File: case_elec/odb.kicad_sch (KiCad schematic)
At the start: 4 parts

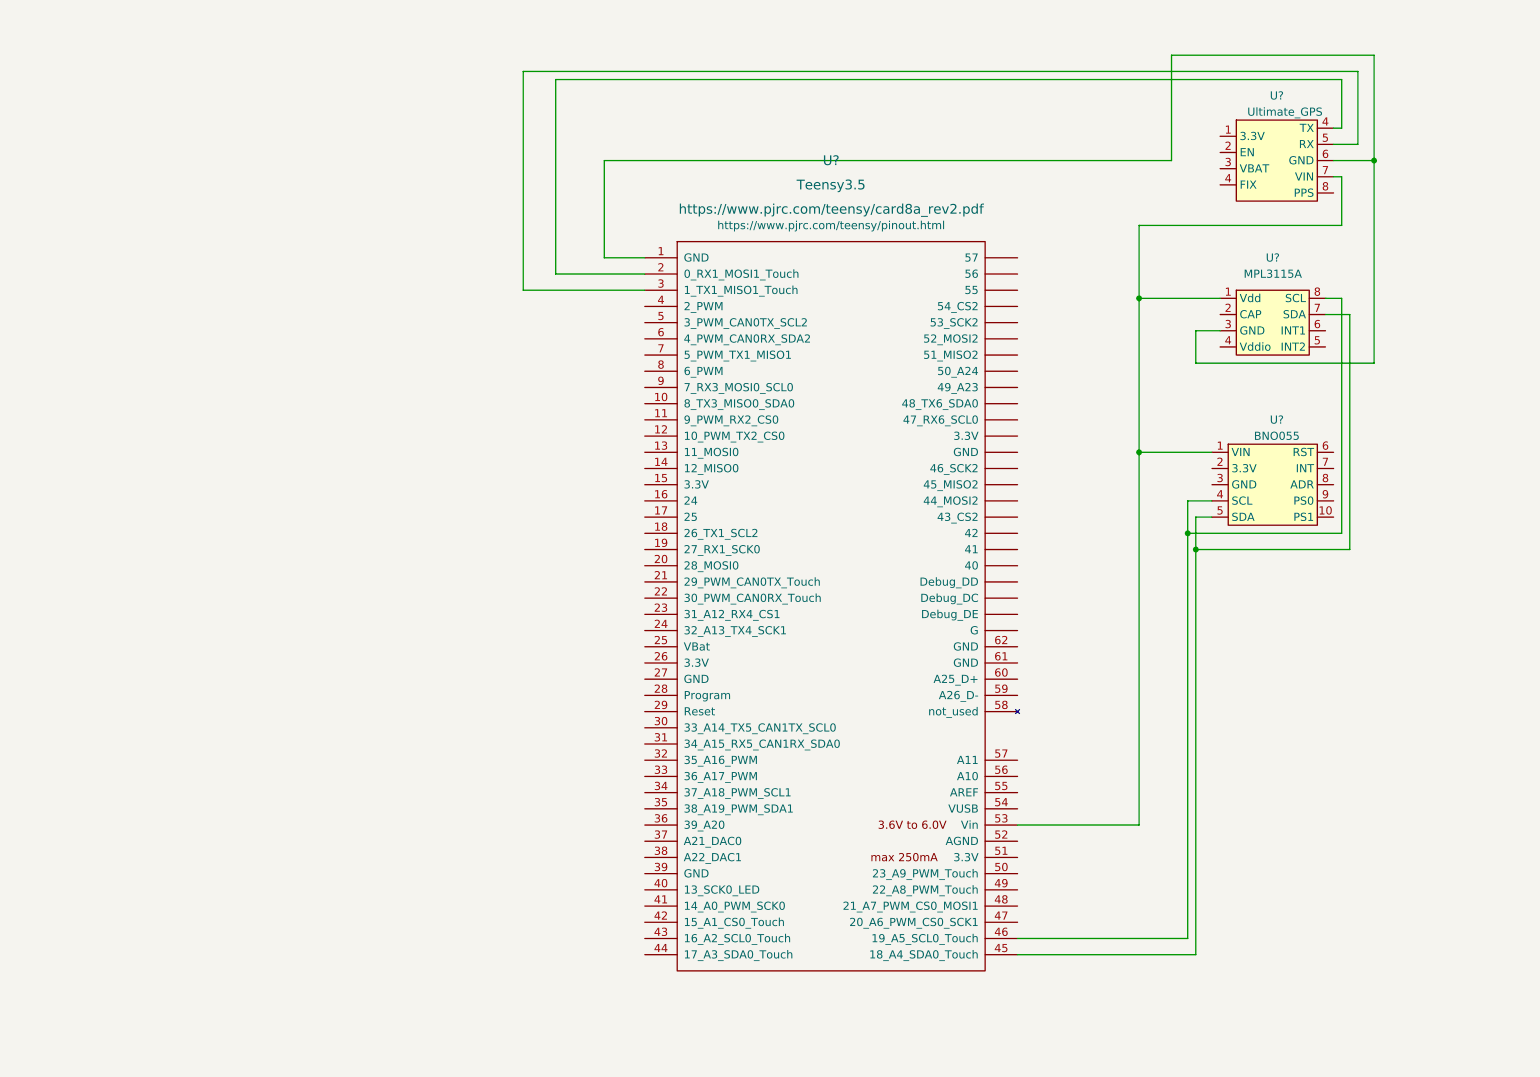
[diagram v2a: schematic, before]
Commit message: Connexion SDA/SCL
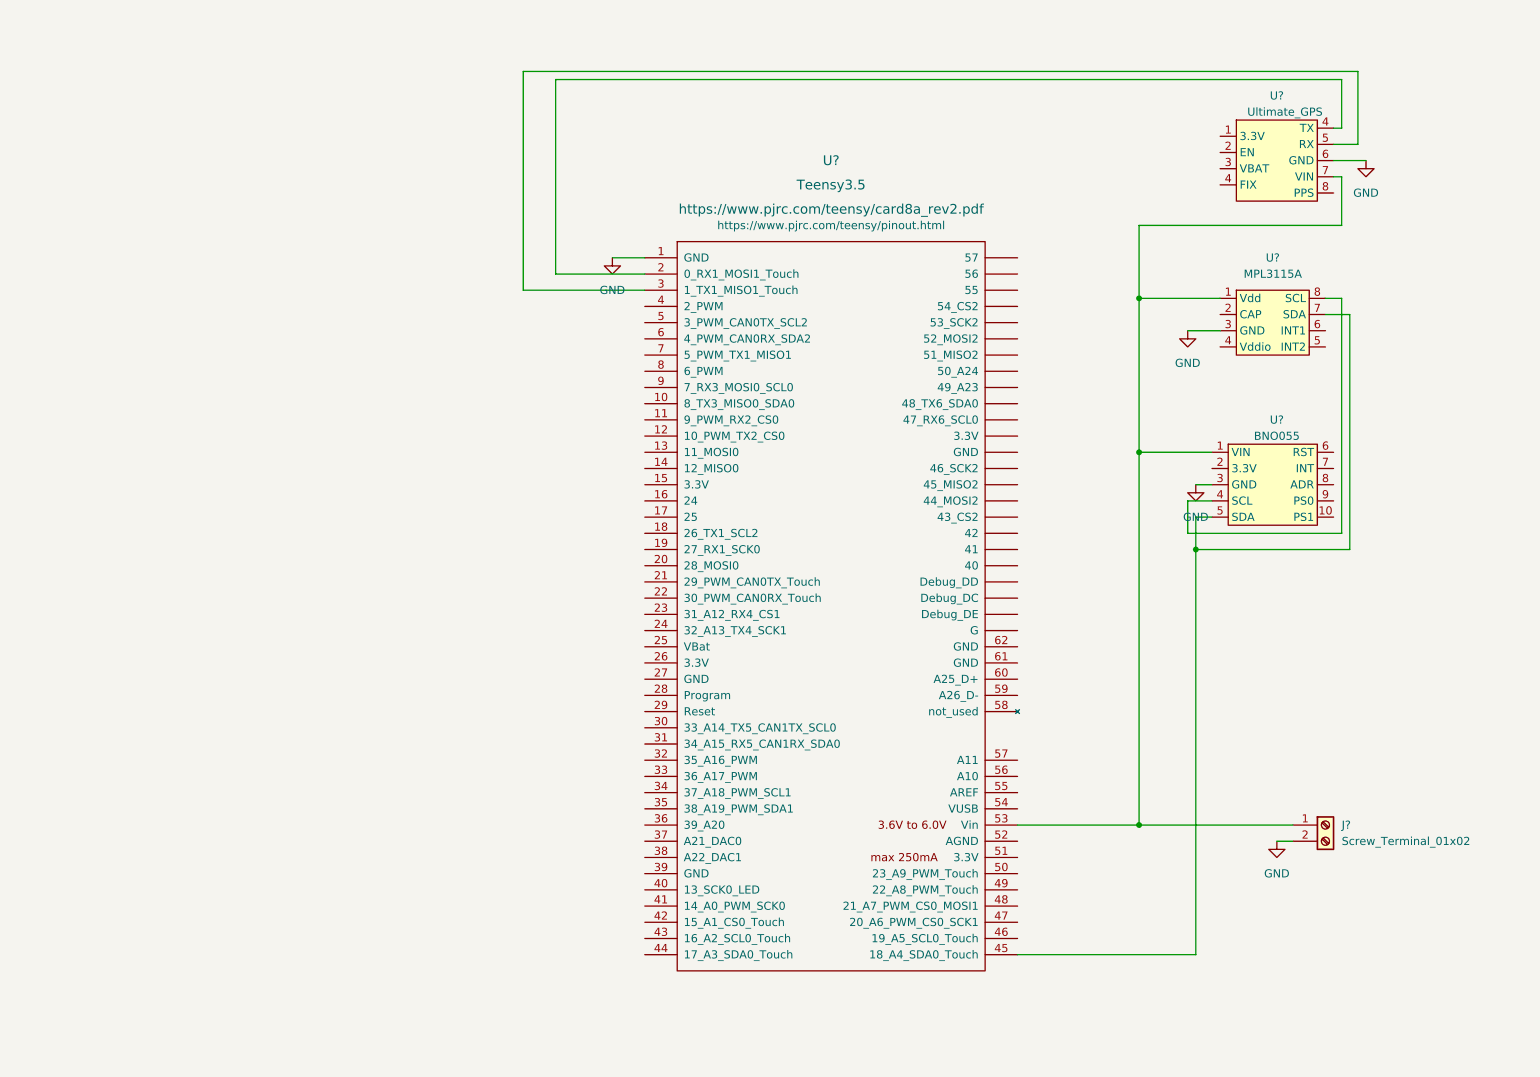
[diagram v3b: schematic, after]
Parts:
- added J?: Screw_Terminal_01x02, symbol Connector:Screw_Terminal_01x02
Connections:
- net at U?.1 (VIN), U?.1 (Vdd), U?.53 (Vin)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: now also J?.1 (Pin_1)
- net GND: now reaches U?.1 (GND), U?.3 (GND), U?.6 (GND)
- net GND: now also U?.3 (GND), J?.2 (Pin_2)
- net at U?.4 (SCL), U?.8 (SCL): no longer U?.46 (19_A5_SCL0_Touch)
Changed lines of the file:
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@@
     (comment 3 "<mohamed-iadh.bani@top-aero.com> <theo.tugaye@top-aero.com>")
   )
-  (junction (at 226.06 40.64) (diameter 0) (color 0 0 0 0)
-  )
   (junction (at 198.12 101.6) (diameter 0) (color 0 0 0 0)
   )
@@
   (junction (at 189.23 86.36) (diameter 0) (color 0 0 0 0)
   )
-  (junction (at 196.85 99.06) (diameter 0) (color 0 0 0 0)
+  (junction (at 189.23 144.78) (diameter 0) (color 0 0 0 0)
   )
   (wire (pts (xy 222.25 101.6) (xy 198.12 101.6))
@@
     (stroke (width 0) (type default) (color 0 0 0 0))
   )
-  (wire (pts (xy 198.12 67.31) (xy 198.12 72.39))
-    (stroke (width 0) (type default) (color 0 0 0 0))
-  )
-  (wire (pts (xy 201.93 67.31) (xy 198.12 67.31))
-    (stroke (width 0) (type default) (color 0 0 0 0))
-  )
   (wire (pts (xy 201.93 62.23) (xy 189.23 62.23))
     (stroke (width 0) (type default) (color 0 0 0 0))
@@
     (stroke (width 0) (type default) (color 0 0 0 0))
   )
-  (wire (pts (xy 198.12 72.39) (xy 226.06 72.39))
-    (stroke (width 0) (type default) (color 0 0 0 0))
-  )
-  (wire (pts (xy 194.31 40.64) (xy 194.31 24.13))
+  (wire (pts (xy 196.85 67.31) (xy 201.93 67.31))
+    (stroke (width 0) (type default) (color 0 0 0 0))
+  )
+  (wire (pts (xy 106.68 55.88) (xy 111.76 55.88))
     (stroke (width 0) (type default) (color 0 0 0 0))
   )
@@
     (stroke (width 0) (type default) (color 0 0 0 0))
   )
-  (wire (pts (xy 194.31 40.64) (xy 105.41 40.64))
-    (stroke (width 0) (type default) (color 0 0 0 0))
-  )
   (wire (pts (xy 97.79 27.94) (xy 220.98 27.94))
     (stroke (width 0) (type default) (color 0 0 0 0))
@@
     (stroke (width 0) (type default) (color 0 0 0 0))
   )
-  (wire (pts (xy 105.41 55.88) (xy 111.76 55.88))
-    (stroke (width 0) (type default) (color 0 0 0 0))
-  )
   (wire (pts (xy 219.71 35.56) (xy 220.98 35.56))
     (stroke (width 0) (type default) (color 0 0 0 0))
   )
-  (wire (pts (xy 226.06 24.13) (xy 226.06 40.64))
-    (stroke (width 0) (type default) (color 0 0 0 0))
-  )
-  (wire (pts (xy 196.85 162.56) (xy 196.85 99.06))
-    (stroke (width 0) (type default) (color 0 0 0 0))
-  )
-  (wire (pts (xy 219.71 40.64) (xy 226.06 40.64))
+  (wire (pts (xy 189.23 144.78) (xy 213.36 144.78))
+    (stroke (width 0) (type default) (color 0 0 0 0))
+  )
+  (wire (pts (xy 198.12 91.44) (xy 200.66 91.44))
     (stroke (width 0) (type default) (color 0 0 0 0))
   )
@@
     (stroke (width 0) (type default) (color 0 0 0 0))
   )
-  (wire (pts (xy 170.18 162.56) (xy 196.85 162.56))
-    (stroke (width 0) (type default) (color 0 0 0 0))
-  )
   (wire (pts (xy 222.25 64.77) (xy 222.25 101.6))
     (stroke (width 0) (type default) (color 0 0 0 0))
@@
     (stroke (width 0) (type default) (color 0 0 0 0))
   )
-  (wire (pts (xy 226.06 40.64) (xy 226.06 72.39))
-    (stroke (width 0) (type default) (color 0 0 0 0))
-  )
   (wire (pts (xy 220.98 50.8) (xy 189.23 50.8))
     (stroke (width 0) (type default) (color 0 0 0 0))
   )
-  (wire (pts (xy 105.41 40.64) (xy 105.41 55.88))
-    (stroke (width 0) (type default) (color 0 0 0 0))
-  )
   (wire (pts (xy 218.44 64.77) (xy 222.25 64.77))
     (stroke (width 0) (type default) (color 0 0 0 0))
   )
-  (wire (pts (xy 194.31 24.13) (xy 226.06 24.13))
-    (stroke (width 0) (type default) (color 0 0 0 0))
-  )
   (wire (pts (xy 220.98 62.23) (xy 220.98 99.06))
     (stroke (width 0) (type default) (color 0 0 0 0))
   )
+  (wire (pts (xy 213.36 147.32) (xy 210.82 147.32))
+    (stroke (width 0) (type default) (color 0 0 0 0))
+  )
   (wire (pts (xy 198.12 96.52) (xy 200.66 96.52))
     (stroke (width 0) (type default) (color 0 0 0 0))
   )
+  (wire (pts (xy 219.71 40.64) (xy 224.79 40.64))
+    (stroke (width 0) (type default) (color 0 0 0 0))
+  )
   (wire (pts (xy 97.79 58.42) (xy 97.79 27.94))
     (stroke (width 0) (type default) (color 0 0 0 0))
+  )
+  (symbol (lib_id "Connector:Screw_Terminal_01x02") (at 218.44 144.78 0) (unit 1)
+    (in_bom yes) (on_board yes) (fields_autoplaced)
+    (property "Reference" "J?" (id 0) (at 220.98 144.7799 0)
+      (effects (font (size 1.27 1.27)) (justify left))
+    )
+    (property "Value" "Screw_Terminal_01x02" (id 1) (at 220.98 147.3199 0)
+      (effects (font (size 1.27 1.27)) (justify left))
+    )
+    (property "Footprint" "" (id 2) (at 218.44 144.78 0)
+      (effects (font (size 1.27 1.27)) hide)
+    )
+    (property "Datasheet" "~" (id 3) (at 218.44 144.78 0)
+      (effects (font (size 1.27 1.27)) hide)
+    )
+    (pin "1")
+    (pin "2")
   )
   (symbol (lib_id "Adafruit_sensors:MPL3115A") (at 214.63 66.04 0) (unit 1)
@@
     (pin "7")
     (pin "8")
+  )
+  (symbol (lib_id "power:GND") (at 106.68 55.88 0) (unit 1)
+    (in_bom yes) (on_board yes) (fields_autoplaced)
+    (property "Reference" "#PWR?" (id 0) (at 106.68 62.23 0)
+      (effects (font (size 1.27 1.27)) hide)
+    )
+    (property "Value" "GND" (id 1) (at 106.68 60.96 0))
+    (property "Footprint" "" (id 2) (at 106.68 55.88 0)
+      (effects (font (size 1.27 1.27)) hide)
+    )
+    (property "Datasheet" "" (id 3) (at 106.68 55.88 0)
+      (effects (font (size 1.27 1.27)) hide)
+    )
+    (pin "1")
+  )
+  (symbol (lib_id "power:GND") (at 224.79 40.64 0) (unit 1)
+    (in_bom yes) (on_board yes) (fields_autoplaced)
+    (property "Reference" "#PWR?" (id 0) (at 224.79 46.99 0)
+      (effects (font (size 1.27 1.27)) hide)
+    )
+    (property "Value" "GND" (id 1) (at 224.79 45.72 0))
+    (property "Footprint" "" (id 2) (at 224.79 40.64 0)
+      (effects (font (size 1.27 1.27)) hide)
+    )
+    (property "Datasheet" "" (id 3) (at 224.79 40.64 0)
+      (effects (font (size 1.27 1.27)) hide)
+    )
+    (pin "1")
+  )
+  (symbol (lib_id "power:GND") (at 198.12 91.44 0) (unit 1)
+    (in_bom yes) (on_board yes) (fields_autoplaced)
+    (property "Reference" "#PWR?" (id 0) (at 198.12 97.79 0)
+      (effects (font (size 1.27 1.27)) hide)
+    )
+    (property "Value" "GND" (id 1) (at 198.12 96.52 0))
+    (property "Footprint" "" (id 2) (at 198.12 91.44 0)
+      (effects (font (size 1.27 1.27)) hide)
+    )
+    (property "Datasheet" "" (id 3) (at 198.12 91.44 0)
+      (effects (font (size 1.27 1.27)) hide)
+    )
+    (pin "1")
   )
   (symbol (lib_id "Teensy:Teensy3.5") (at 140.97 110.49 0) (unit 1)
@@
     (pin "~")
   )
+  (symbol (lib_id "power:GND") (at 210.82 147.32 0) (unit 1)
+    (in_bom yes) (on_board yes) (fields_autoplaced)
+    (property "Reference" "#PWR?" (id 0) (at 210.82 153.67 0)
+      (effects (font (size 1.27 1.27)) hide)
+    )
+    (property "Value" "GND" (id 1) (at 210.82 152.4 0))
+    (property "Footprint" "" (id 2) (at 210.82 147.32 0)
+      (effects (font (size 1.27 1.27)) hide)
+    )
+    (property "Datasheet" "" (id 3) (at 210.82 147.32 0)
+      (effects (font (size 1.27 1.27)) hide)
+    )
+    (pin "1")
+  )
   (symbol (lib_id "Adafruit_sensors:Ultimate_GPS") (at 210.82 41.91 0) (unit 1)
     (in_bom yes) (on_board yes)
@@
     (pin "9")
   )
+  (symbol (lib_id "power:GND") (at 196.85 67.31 0) (unit 1)
+    (in_bom yes) (on_board yes) (fields_autoplaced)
+    (property "Reference" "#PWR?" (id 0) (at 196.85 73.66 0)
+      (effects (font (size 1.27 1.27)) hide)
+    )
+    (property "Value" "GND" (id 1) (at 196.85 72.39 0))
+    (property "Footprint" "" (id 2) (at 196.85 67.31 0)
+      (effects (font (size 1.27 1.27)) hide)
+    )
+    (property "Datasheet" "" (id 3) (at 196.85 67.31 0)
+      (effects (font (size 1.27 1.27)) hide)
+    )
+    (pin "1")
+  )
   (sheet_instances
     (path "/" (page "1"))
   )
   (symbol_instances
+    (path "/54b19888-c4a4-406d-a404-1f5cb4236a7c"
+      (reference "#PWR?") (unit 1) (value "GND") (footprint "")
+    )
+    (path "/5bd4d6d4-a0d9-47c1-b4c1-4ee309d230a5"
+      (reference "#PWR?") (unit 1) (value "GND") (footprint "")
+    )
+    (path "/6b3f866d-2465-4dbb-8687-636966a4dae8"
+      (reference "#PWR?") (unit 1) (value "GND") (footprint "")
+    )
+    (path "/7e02d6a6-30db-42e9-891a-0e8fa87d26cc"
+      (reference "#PWR?") (unit 1) (value "GND") (footprint "")
+    )
+    (path "/df1f09bb-708e-40da-ae95-fe7d068e7402"
+      (reference "#PWR?") (unit 1) (value "GND") (footprint "")
+    )
+    (path "/39ee107a-0aa1-4a95-84c1-71d5198b1407"
+      (reference "J?") (unit 1) (value "Screw_Terminal_01x02") (footprint "")
+    )
     (path "/4324021c-adf2-48f1-8a00-7ea1c3478302"
       (reference "U?") (unit 1) (value "MPL3115A") (footprint "")

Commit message: Ajouts de composants et connexions
- molex
- interrupteurs x2
- module lora
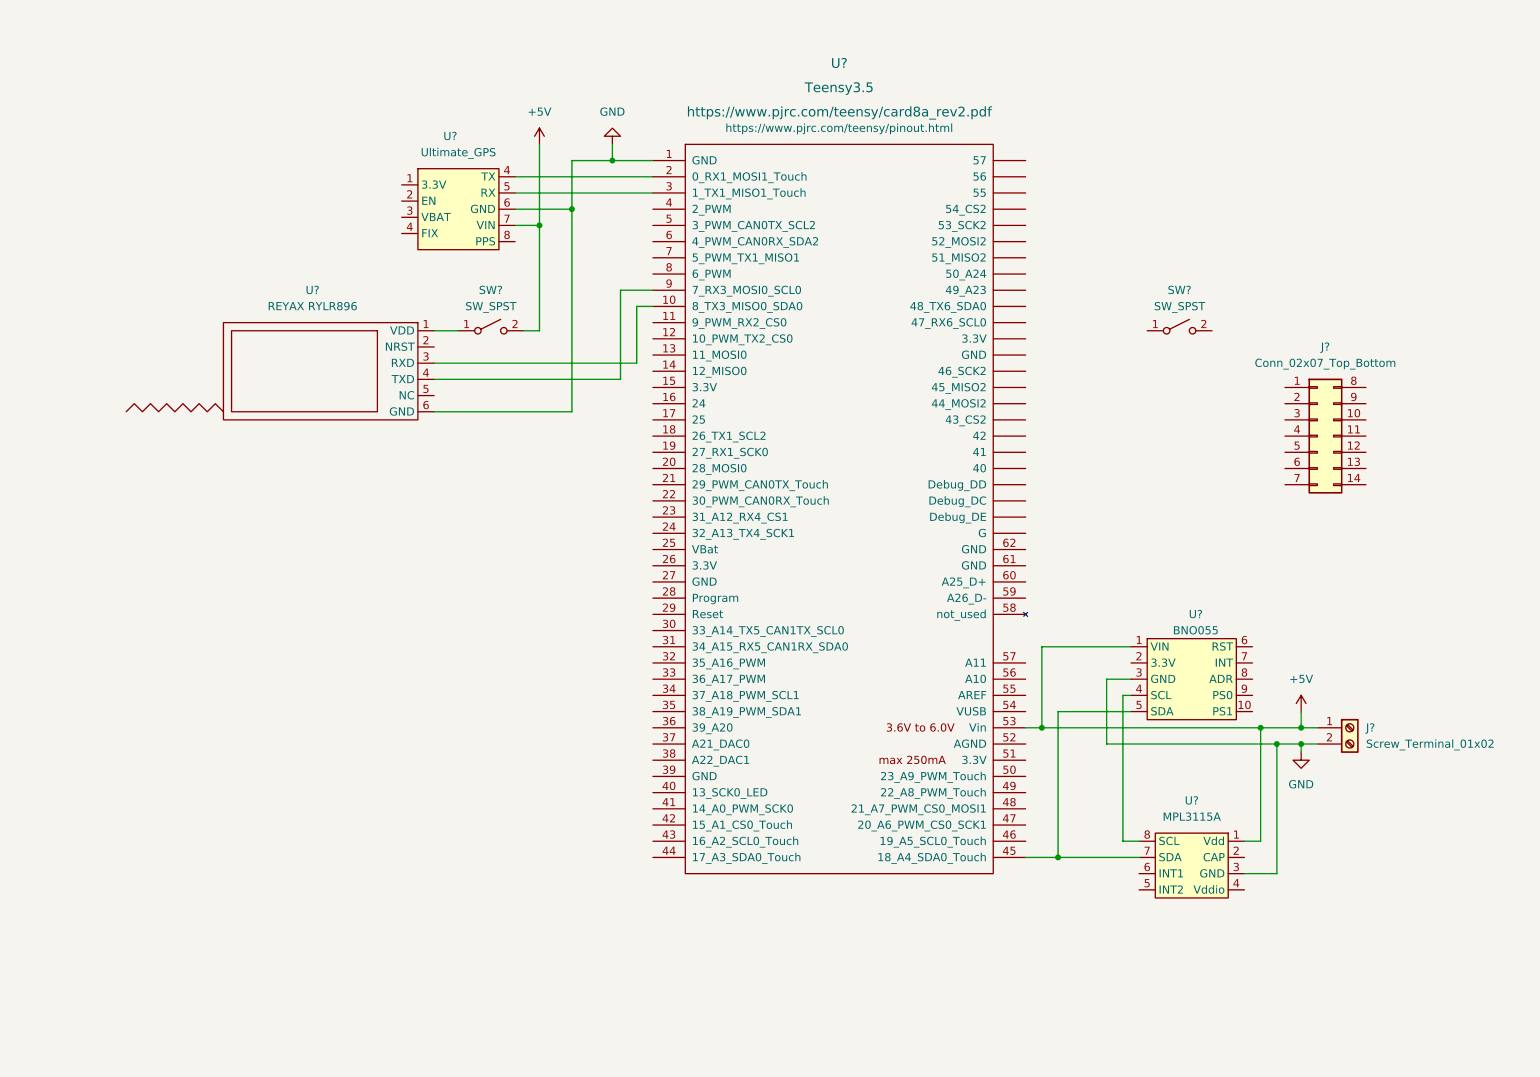
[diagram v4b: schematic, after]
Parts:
- added J?: Conn_02x07_Top_Bottom, symbol Connector_Generic:Conn_02x07_Top_Bottom
- added SW? (x2): SW_SPST, symbol Switch:SW_SPST
- added U?: REYAX RYLR896, symbol reyax_rylr896:REYAX RYLR896
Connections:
- net GND: now also U?.6 (GND)
- net +5V: now reaches J?.1 (Pin_1), U?.1 (VIN), U?.1 (Vdd), U?.53 (Vin), U?.7 (VIN)
- net +5V: now also SW?.2 (B)
- net at U?.10 (8_TX3_MISO0_SDA0): now also U?.3 (RXD)
- net at U?.9 (7_RX3_MOSI0_SCL0): now also U?.4 (TXD)
- new net: SW?.1 (A), U?.1 (VDD)
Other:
- company: Sorbonne Université - Top Aéro -> Top Aéro
- moved on the sheet: J?, U?

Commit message: complétion du schéma électrique
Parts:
- removed J?: Screw_Terminal_01x02, symbol Connector:Screw_Terminal_01x02
- removed SW?: SW_SPST, symbol Switch:SW_SPST
- removed U?: MPL3115A, symbol Adafruit_sensors:MPL3115A
- removed U?: BNO055, symbol Adafruit_sensors:BNO055
- added J1: Screw_Terminal_01x02, symbol Connector:Screw_Terminal_01x02
- added SW1: SW_SPST, symbol Switch:SW_SPST
- added U2: BNO055, symbol Adafruit_sensors:BNO055
- added U3: MPL3115A, symbol Adafruit_sensors:MPL3115A
- U1: renamed from U?; Command (none) -> https://reyax.com/wp-content/uploads/2019/12/LoRa-AT-Comman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
- gave numbers to parts that had none: 4
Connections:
- net +5V: now also SW1.2 (B), U2.1 (VIN), U3.1 (Vdd)
- net GND: now also J1.2 (Pin_2), U2.3 (GND), U3.3 (GND)
- net A4: now reaches U5.45 (18_A4_SDA0_Touch)
- net A4: now also J2.5 (Pin_5)
- net A0: now reaches J2.1 (Pin_1)
- net A0: now also U5.41 (14_A0_PWM_SCK0)
- net A9: now reaches J2.10 (Pin_10)
- net A9: now also U5.50 (23_A9_PWM_Touch)
- net A19: now reaches J2.11 (Pin_11)
- net A19: now also U5.35 (38_A19_PWM_SDA1)
- net A20: now reaches J2.12 (Pin_12)
- net A20: now also U5.36 (39_A20)
- net A21: now reaches J2.13 (Pin_13)
- net A21: now also U5.37 (A21_DAC0)
- net A22: now reaches J2.14 (Pin_14)
- net A22: now also U5.38 (A22_DAC1)
- net A1: now reaches J2.2 (Pin_2)
- net A1: now also U5.42 (15_A1_CS0_Touch)
- net A2: now reaches J2.3 (Pin_3)
- net A2: now also U5.43 (16_A2_SCL0_Touch)
- net A3: now reaches J2.4 (Pin_4)
- net A3: now also U5.44 (17_A3_SDA0_Touch)
- net A5: now reaches J2.6 (Pin_6)
- net A5: now also U5.46 (19_A5_SCL0_Touch)
- net A6: now reaches J2.7 (Pin_7)
- net A6: now also U5.47 (20_A6_PWM_CS0_SCK1)
- net A7: now reaches J2.8 (Pin_8)
- net A7: now also U5.48 (21_A7_PWM_CS0_MOSI1)
- net A8: now reaches J2.9 (Pin_9)
- net A8: now also U5.49 (22_A8_PWM_Touch)
- net at U5.10 (8_TX3_MISO0_SDA0): now also U2.5 (SDA), U3.7 (SDA); no longer U1.3 (RXD)
- net at U5.23 (31_A12_RX4_CS1): now also U1.4 (TXD)
- net at U5.24 (32_A13_TX4_SCK1): now also U1.3 (RXD)
- net at U5.9 (7_RX3_MOSI0_SCL0): now also U2.4 (SCL), U3.8 (SCL); no longer U1.4 (TXD)
- new net: J1.1 (Pin_1), SW1.1 (A)
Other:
- moved on the sheet: J2, SW2, U4, U5
